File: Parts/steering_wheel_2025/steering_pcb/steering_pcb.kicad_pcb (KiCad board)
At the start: 2 copper layers, 102 x 102 mm, 195 parts, among them J0 Quick_connector, J1 Button 1 molex-µfit connector, J10 Button 1 molex-µfit connector, J11 Button 1 molex-µfit connector, J12 Button 1 molex-µfit connector, J13 PINHD_1x1_Male, J14 Conn_01x04_Pin, J15 CAN pin header, J16 Conn_01x01_Pin, J2 Button 1 molex-µfit connector, J3 Button 1 molex-µfit connector, J4 Button 1 molex-µfit connector, J5 Button 1 molex-µfit connector, J6 Button 1 molex-µfit connector, J7 Button 1 molex-µfit connector, J8 Button 1 molex-µfit connector, J9 Button 1 molex-µfit connector, Q1 BSS138BKS, Q10 2N7002DW, Q11 2N7002DW, Q12 2N7002DW, Q13 2N7002DW, Q14 2N7002DW, Q15 2N7002DW, Q16 2N7002DW, Q17 2N7002DW, Q18 2N7002DW, Q19 2N7002DW, Q2 2N7002DW, Q20 2N7002DW, Q21 2N7002DW, Q3 2N7002DW, Q4 BS170, Q5 2N7002DW, Q6 BSS138BKS, Q7 2N7002DW, Q8 2N7002DW, Q9 2N7002DW, SW1 Push_Button, U1 MCP2515-xSO, U2 TPS5430DDA, U3 TPS5430DDA, U5 ISM330DHCX, U6 TJA1051T-3, Y1 16MHz

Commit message: Error fixing with kicad_dru, and silkscreeen updates. TO-DO: BOM to basic
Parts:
- added ?: , , F.Cu at (205.4, 101.5)
- added ?: , , F.Cu at (205.1, 90.2)
- added ?: , , F.Cu at (209.8, 100.1)
- C17: footprint PCM_Capacitor_Tantalum_SMD_AKL:CAP_10TPB220ML -> ROAST:CAP_10TPB220ML
- D1, D10, D11, D12, D2, D3, D4, D5, D6, D7, D8, D9, Q1, Q10, Q11, Q12, Q13, Q14, Q15, Q16, Q17, Q18, Q19, Q2, Q20, Q21, Q3, Q5, Q6, Q7, Q8, Q9: footprint PCM_Package_TO_SOT_SMD_AKL:SOT-363_SC-70-6 -> Package_TO_SOT_SMD:SOT-363_SC-70-6
- D14: footprint PCM_Package_TO_SOT_SMD_AKL:SOT-23 -> Package_TO_SOT_SMD:SOT-23
- D15: footprint PCM_Diode_SMD_AKL:D_SMC -> Diode_SMD:D_SMC
- J0: footprint Connector_PinSocket_2.54mm:PinSocket_2x02_P2.54mm_Vertical -> Connector_Molex:Molex_Micro-Fit_3.0_43045-0412_2x02_P3.00mm_Vertical
- J14: footprint Connector_PinHeader_1.00mm:PinHeader_1x04_P1.00mm_Vertical -> Connector_PinHeader_2.54mm:PinHeader_1x04_P2.54mm_Vertical; moved to B.Cu
- Q4: footprint PCM_Package_TO_SOT_THT_AKL:TO-92_Inline_Wide_DGS -> Package_TO_SOT_THT:TO-92_Inline_Wide
- SW1: value Push_Button -> Reset Button
- moved J14 69.7 mm to (230.9, 41.9), turned to 90 degrees
- moved R86 68.2 mm to (231.6, 45.5)
- moved R87 68.1 mm to (228.3, 45.5)
- moved R88 68.1 mm to (226.1, 45.5)
- moved R89 67.9 mm to (222.7, 45.5)
- moved J16 67.7 mm to (233.4, 41.9), turned to 180 degrees
- moved JP8 11.5 mm to (170.9, 121.4)
- moved C7 5.76 mm to (183.8, 137.8)
- moved Q4 5.60 mm to (176.0, 132.3), turned to 90 degrees
- moved R2 5.02 mm to (209.2, 100.1)
- moved C12 5.02 mm to (204.9, 103.8)
- moved C14 5.02 mm to (201.0, 101.9)
- moved C15 5.02 mm to (207.9, 104.7)
- moved D16 5.02 mm to (203.1, 90.7)
- moved JP4 5.02 mm to (206.1, 101.5)
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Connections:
- A1 pad 5V2: MCU_5V -> +5V_MCU
- J0 pad 1: GND -> +12V
- J0 pad 2: CAN_H -> GND
- J0 pad 3: +12V -> CAN_H
- J15 pad 5: MCU_5V -> +5V_MCU
- R10 pad 1: +5V -> +5V_MCU
- R13 pad 1: +5V -> +5V_MCU
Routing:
- net +5V_MCU: track 89.3 -> 179.2 mm, vias 1 -> 5
- net Net-(J14-Pin_4): track 5.58 -> 91.1 mm
- net Net-(J14-Pin_3): track 5.46 -> 88.7 mm
- net Net-(J14-Pin_2): track 5.29 -> 87.4 mm
- net Net-(J14-Pin_1): track 5.72 -> 87.0 mm
- net GND: track 41.9 -> 55.0 mm, vias 68 -> 161
- net MCU_5V: track 10.1 -> 0.00 mm
- net CAN_L: track 23.8 -> 29.8 mm
- net button3_2: track 20.4 -> 26.1 mm
- net Net-(U1-RXCAN): track 15.7 -> 21.0 mm
- net Net-(U1-TXCAN): track 19.4 -> 24.6 mm
- net CAN_H: track 25.4 -> 30.0 mm
- net +3.3V: track 104.5 -> 108.7 mm
- net +5V: track 3.34 -> 7.39 mm
- net LED_PWM: track 278.0 -> 282.0 mm
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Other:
- board text added: "36"
- board text added: "38"
- board text added: "40"
- board text added: "CAN power solder jumper"
- board text added: "GPIO34"
- board text added: "Gyroscope Power solder jumper"
- board text added: "LED PWM out"
- board text added: "Reset Button"
- board text added: "Solar car - Steering wheel 15th july 2025 s224000, s223986 Rev 1.0"
- board text added: "Solder jumper CAN reset"
- board text added: "arduino +5V"
- board text added: "i2c address OC: 0x6A SC: 0x6B"

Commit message: board update
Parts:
- removed ? (x3): , 
- removed C12, C14, C15: 14pF, Capacitor_SMD:C_0805_2012Metric_Pad1.18x1.45mm_HandSolder
- removed D13: B220-13-F, Diode_SMD:D_SMC
- removed D15: 30BQ040, Diode_SMD:D_SMC
- removed Q1, Q6: BSS138BKS, Package_TO_SOT_SMD:SOT-363_SC-70-6
- removed R5: FRC0402F2101TS, Resistor_SMD:R_0402_1005Metric_Pad0.72x0.64mm_HandSolder
- removed R7: 3.24k, Resistor_SMD:R_0402_1005Metric_Pad0.72x0.64mm_HandSolder
- added C18: 20pF, Capacitor_SMD:C_0805_2012Metric_Pad1.18x1.45mm_HandSolder, F.Cu at (205.0, 103.9)
- added C19: 20pF, Capacitor_SMD:C_0805_2012Metric_Pad1.18x1.45mm_HandSolder, F.Cu at (207.9, 104.9)
- added C20: 20pF, Capacitor_SMD:C_0805_2012Metric_Pad1.18x1.45mm_HandSolder, F.Cu at (200.9, 101.9)
- added D18: ~, Diode_SMD:D_SMA, F.Cu at (226.3, 132.6)
- added D19: ~, Diode_SMD:D_SMA, F.Cu at (195.6, 127.8)
- added R90: 200k, Resistor_SMD:R_0402_1005Metric_Pad0.72x0.64mm_HandSolder, F.Cu at (195.1, 137.9)
- added R91: 3.3k, Resistor_SMD:R_0402_1005Metric_Pad0.72x0.64mm_HandSolder, F.Cu at (195.1, 139.2)
- added R92: 2.2k, Resistor_SMD:R_0402_1005Metric_Pad0.72x0.64mm_HandSolder, F.Cu at (227.3, 121.6)
- added R93: 47k, Resistor_SMD:R_0402_1005Metric_Pad0.72x0.64mm_HandSolder, F.Cu at (228.3, 121.6)
- C1, C2: value 15pF -> 20pF
- C10, C11, C16, C3, C6, C8: value GRM32ER61E226KE15L -> 22uF; footprint Capacitor_SMD:C_1210_3225Metric_Pad1.33x2.70mm_HandSolder -> Capacitor_SMD:C_1206_3216Metric_Pad1.33x1.80mm_HandSolder
- C17: value 10TPB220ML -> 220uF
- C7: value 220uF -> 330uF
- D16, D17: value KT-0603R -> ~
- J1, J10, J11, J12, J2, J3, J4, J5, J6, J7, J8, J9: value Button 1 molex-µfit connector -> molex-µfit connector
- R17, R21, R27, R33, R39, R45, R51, R57, R63, R69, R75, R81: value 180 -> 100
- SW1: value Reset Button -> Push_Button
- moved R89 0.09 mm to (222.8, 45.5)
- moved R86 0.09 mm to (231.5, 45.5)
- turned J16 to 0 degrees
- turned U3 to 0 degrees
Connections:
- C9 pad 1: Net-(U3-BOOT) -> Net-(U3-VIN)
- C9 pad 2: Net-(D13-K) -> Net-(D18-K)
- J0 pad 1: +12V -> Net-(F1-Pad1)
- L3 pad 1: Net-(D13-K) -> Net-(D18-K)
- R4 pad 2: Net-(U3-VSENSE) -> Net-(U3-EN)
- U3 pad 1: Net-(U3-BOOT) -> +12V
- U3 pad 4: Net-(U3-VSENSE) -> unconnected-(U3-VSENSE-Pad4)
- U3 pad 5: unconnected-(U3-EN-Pad5) -> Net-(U3-EN)
- U3 pad 6: GND -> unconnected-(U3-GND-Pad6)
- U3 pad 7: +12V -> Net-(U3-VIN)
- U3 pad 8: Net-(D13-K) -> unconnected-(U3-PH-Pad8)
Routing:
- net Net-(D13-K): track 40.3 -> 0.00 mm
- net Net-(D18-K): track 0.00 -> 23.4 mm
- net Net-(U3-EN): track 0.00 -> 13.5 mm
- net Net-(U3-VIN): track 0.00 -> 6.81 mm, vias 0 -> 3
- net GND: track 55.0 -> 60.5 mm, vias 161 -> 168
- net Net-(U3-VSENSE): track 5.31 -> 0.00 mm
- net Net-(U3-BOOT): track 3.12 -> 0.00 mm
- net Net-(U2-VSENSE): track 6.30 -> 9.05 mm
- net Net-(D19-K): track 30.3 -> 27.8 mm
- net +12V: track 93.9 -> 95.4 mm
- net +7V: track 398.1 -> 399.2 mm
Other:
- board text added: "ROAST"
- board text added: "Solar Car - Steering wheel 1st August 2025 s224000, s223986 Rev 1.0"
- board text added: "molex-µfit connector"
- board text removed: "Solar car - Steering wheel 15th july 2025 s224000, s223986 Rev 1.0"

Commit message: PCB_Remake
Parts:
- moved R55 0.13 mm to (185.2, 55.9)
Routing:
- net GND: track 60.5 -> 59.3 mm, vias 168 -> 165

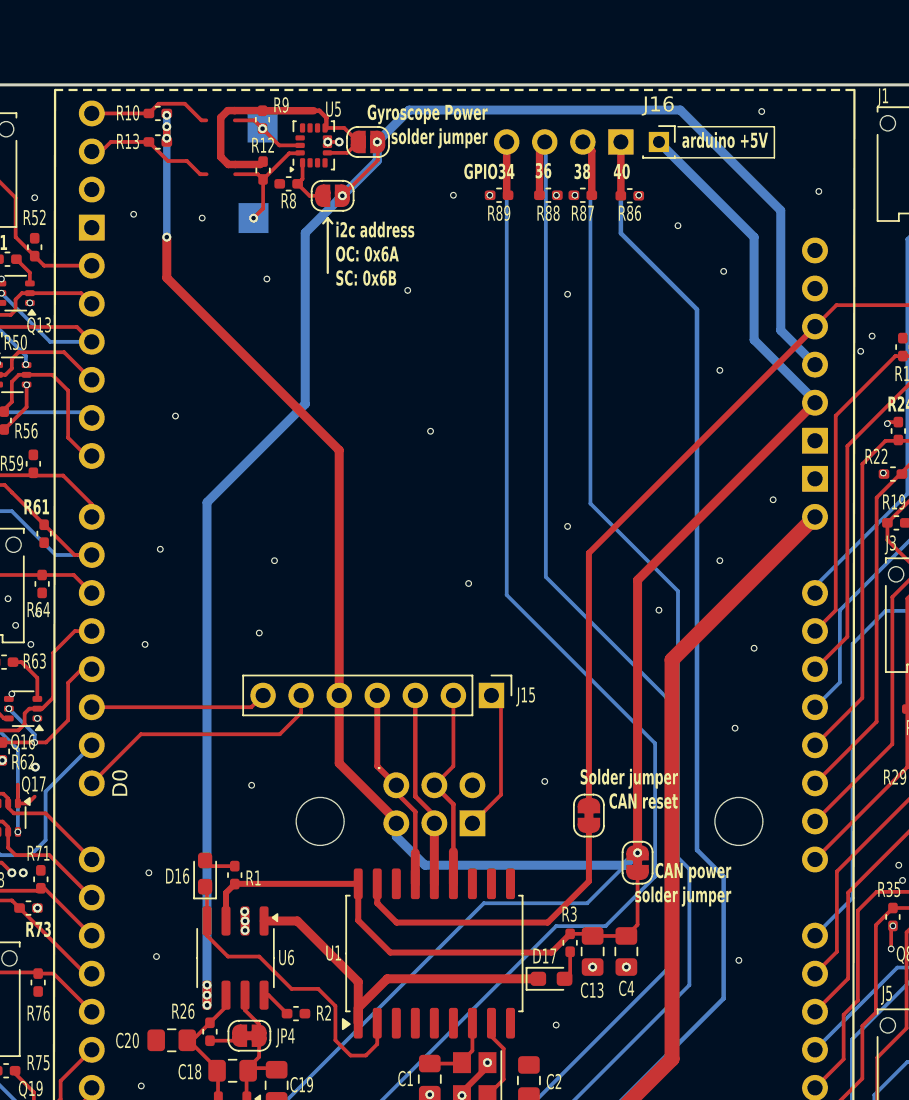
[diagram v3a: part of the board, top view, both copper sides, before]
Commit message: Rename folders for consistency
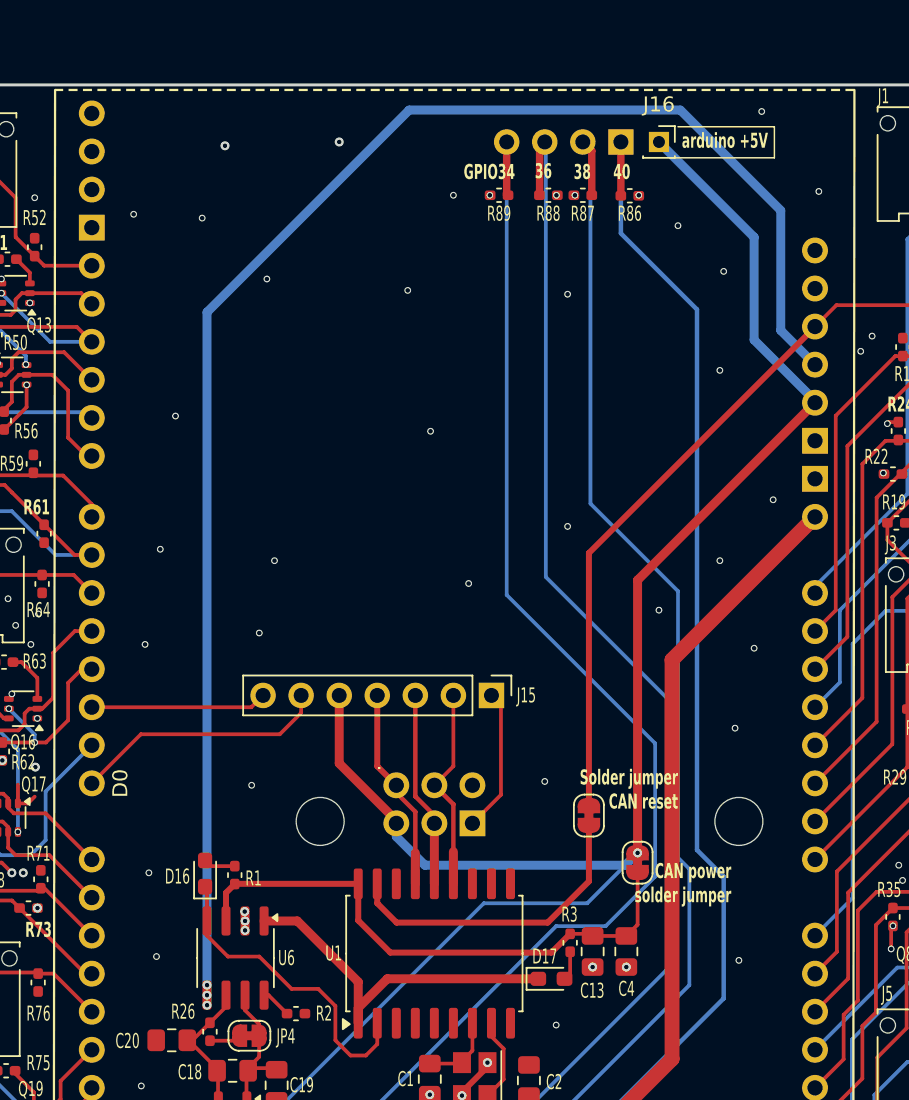
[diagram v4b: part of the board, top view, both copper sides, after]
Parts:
- removed JP1, JP6: ~, Jumper:SolderJumper-2_P1.3mm_Open_RoundedPad1.0x1.5mm
- removed R10, R12, R13, R8, R9: 10k, Resistor_SMD:R_0402_1005Metric_Pad0.72x0.64mm_HandSolder
- removed TP_SCL3v1: SCL TestPoint, TestPoint:TestPoint_Pad_2.0x2.0mm
- removed TP_SDA3v1: 3v SDA TestPoint, TestPoint:TestPoint_Pad_2.0x2.0mm
- removed U5: ISM330DHCX, Package_LGA:LGA-14_3x2.5mm_P0.5mm_LayoutBorder3x4y
- D16, D17: value ~ -> KT-0603R
- D18, D19: value ~ -> SS34
- J1, J10, J11, J12, J2, J3, J4, J5, J6, J7, J8, J9: value molex-µfit connector -> Button 1 molex-µfit connector
- R1, R3: value 1k -> 1kΩ
- R11, R15, R16, R18, R19, R2, R22, R23, R24, R25, R28, R29, R31, R32, R35, R36, R37, R38, R4, R40, R41, R43, R44, R47, R48, R49, R50, R52, R53, R55, R56, R59, R6, R60, R61, R62, R64, R65, R67, R68, R71, R72, R73, R74, R76, R77, R79, R80, R83, R84, R85, R86, R87, R88, R89: value 10k -> 10kΩ
- R14, R17, R20, R21, R27, R30, R33, R34, R39, R42, R45, R46, R51, R54, R57, R58, R63, R66, R69, R70, R75, R78, R81, R82: value 100 -> 100Ω
- R26: value 120 -> 120Ω
- R90: value 200k -> 200kΩ
- R91: value 3.3k -> 3.3kΩ
- R92: value 2.2k -> 2.2kΩ
- R93: value 47k -> 47kΩ
- U2, U3: value TPS5430DDA -> TPS5430DDAR
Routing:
- net +5V_MCU: track 179.2 -> 134.6 mm, vias 5 -> 1
- net Net-(JP6-A): track 18.9 -> 0.00 mm
- net MCU_SDA: track 8.82 -> 0.00 mm
- net MCU_SCL: track 8.83 -> 0.18 mm
- net SDA_3V: track 8.06 -> 0.00 mm, vias 1 -> 0
- net SCL_3V: track 5.05 -> 0.00 mm, vias 1 -> 0
- net +3.3V: track 108.7 -> 104.1 mm, vias 5 -> 3
- net SDO: track 3.56 -> 0.00 mm
- net GND: track 59.3 -> 58.5 mm
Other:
- board text removed: "Gyroscope Power solder jumper"
- board text removed: "i2c address OC: 0x6A SC: 0x6B"
